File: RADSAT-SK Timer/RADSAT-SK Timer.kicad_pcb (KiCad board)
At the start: 2 copper layers, 90.2 x 95.9 mm, 116 parts, among them J101 Conn_02x26_Odd_Even, J103 Conn_02x26_Odd_Even, J201 Conn_01x07, J202 Conn_01x05, J203 Conn_01x03, J204 Conn_01x02, J205 Conn_01x02, J206 Conn_01x02, J210 ZX62WRD-B-5PC, Q101 IRLML2060, Q102 IRLML2060, Q103 IRLML2060, Q104 IRLML2060, Q105 IRLML2060, Q106 IRLML2060, Q107 IRLML2060, Q108 IRLML2060, Q109 IRLML2060, Q201 IRLML2060, Q202 IRLML2060, Q203 IRLML2060, Q204 PJFET, Q205 PJFET, Q206 PJFET, SW201 SW_Push, SW202 SW_Push, SW203 SW_Push, SW204 SW_Push, SW205 SW_Push, SW206 SW_Push, U101 LM397MF, U102 LM397MF, U103 LM397MF, U104 CD4052B, U202 LTC3440EMSPBF, U210 CPC1117N

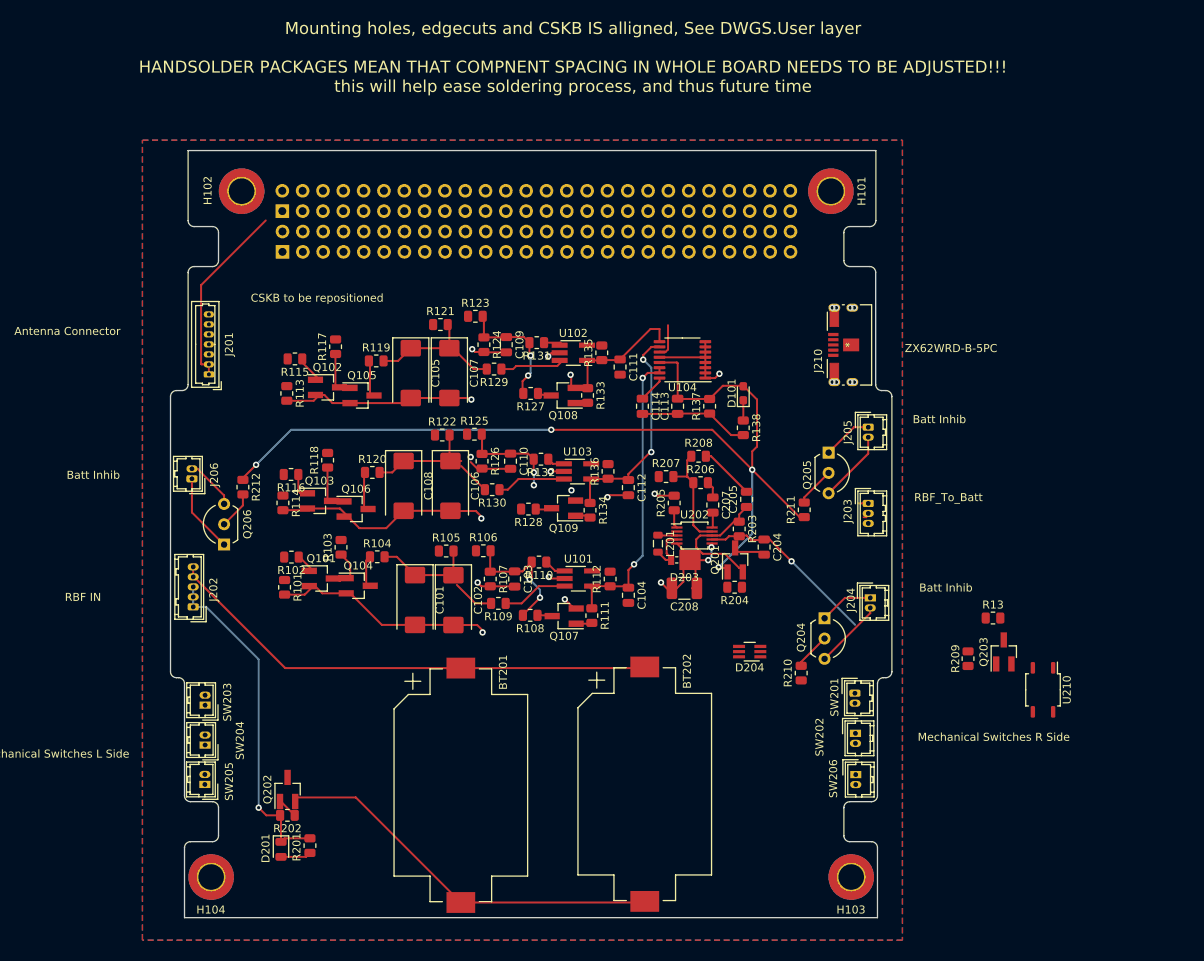
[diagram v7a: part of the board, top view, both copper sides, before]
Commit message: actually did the other relays for the inhibits, played around with layout stuff
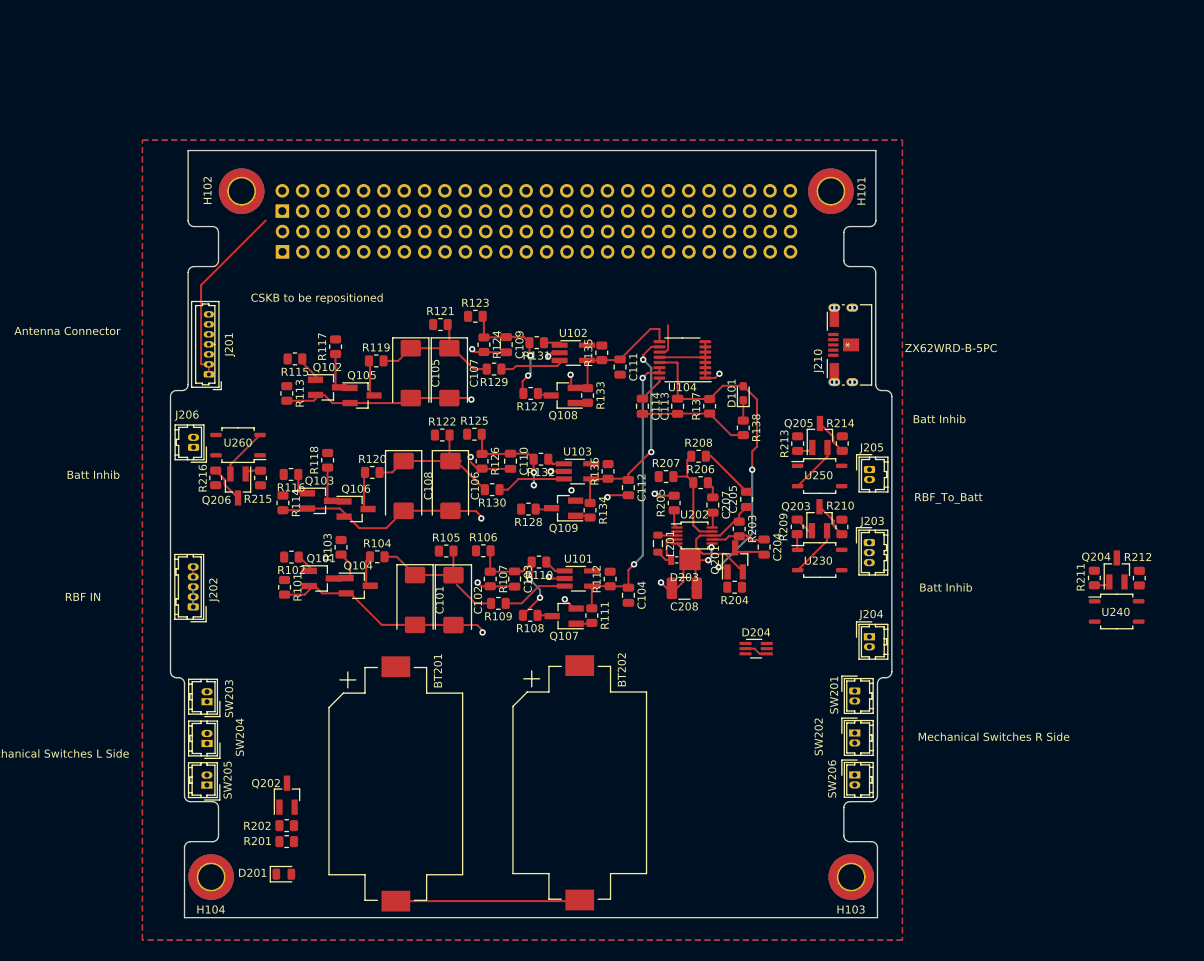
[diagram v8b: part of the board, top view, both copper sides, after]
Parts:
- removed the R210 at (113.7, 115.3)
- added R213: 100, Resistor_SMD:R_0805_2012Metric, F.Cu at (113.2, 86.6)
- added R214: 1k, Resistor_SMD:R_0805_2012Metric, F.Cu at (118.8, 86.6)
- added R215: 100, Resistor_SMD:R_0805_2012Metric, F.Cu at (46.1, 90.9)
- added R216: 1k, Resistor_SMD:R_0805_2012Metric, F.Cu at (40.5, 90.9)
- added U240: CPC1117N, Package_SO:SOP-4_3.8x4.1mm_P2.54mm, F.Cu at (153.1, 107.6)
- added U250: CPC1117N, Package_SO:SOP-4_3.8x4.1mm_P2.54mm, F.Cu at (116.0, 90.7)
- added U260: CPC1117N, Package_SO:SOP-4_3.8x4.1mm_P2.54mm, F.Cu at (43.3, 86.8)
- Q204, Q205, Q206: value PJFET -> IRLML2060; footprint Package_TO_SOT_THT:TO-92L_Inline_Wide -> Package_TO_SOT_SMD:SOT-23_Handsoldering
- R212: value 100 -> 1k
- moved R212 112.6 mm to (155.9, 103.4), turned to 90 degrees
- moved R211 37.3 mm to (150.3, 103.4), turned to 270 degrees
- moved Q204 37.0 mm to (153.1, 102.4), turned to 90 degrees
- moved U230 32.3 mm to (116.0, 101.2), turned to 0 degrees
- moved Q203 28.4 mm to (116.0, 96.0)
- moved R209 27.0 mm to (113.2, 97.0), turned to 90 degrees
- moved R210 22.1 mm to (118.8, 97.1), turned to 90 degrees
- moved BT201 8.13 mm to (63.0, 129.2)
- moved BT202 8.13 mm to (86.0, 129.0)
- moved Q206 7.53 mm to (43.3, 91.9), turned to 270 degrees
- moved J205 5.29 mm to (122.2, 89.9)
- moved J203 4.90 mm to (122.2, 99.0)
- moved J204 4.86 mm to (122.2, 110.8)
- moved J206 3.93 mm to (37.7, 87.1)
- moved D201 3.12 mm to (49.0, 140.5), turned to 0 degrees
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- renumbered R13 to R210, U210 to U230
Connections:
- Q204 pad 1: Net-(J204-Pad1) -> Net-(Q204-Pad1)
- Q204 pad 3: Net-(J204-Pad2) -> Net-(Q204-Pad3)
- Q205 pad 1: Net-(J205-Pad1) -> Net-(Q205-Pad1)
- Q205 pad 3: Net-(J205-Pad2) -> Net-(Q205-Pad3)
- Q206 pad 1: Net-(J206-Pad1) -> Net-(Q206-Pad1)
- Q206 pad 3: Net-(J206-Pad2) -> Net-(Q206-Pad3)
- R210 pad 1: GND -> Net-(Q203-Pad3)
- R210 pad 2: Net-(Q203-Pad3) -> GND
- R211 pad 2: Net-(Q205-Pad2) -> Net-(Q204-Pad1)
- R212 pad 1: BUS_EN -> Net-(Q204-Pad3)
- R212 pad 2: Net-(Q206-Pad2) -> GND
- SW201 pad 1: Net-(C204-Pad1) -> Net-(SW201-Pad1)
- SW201 pad 2: Net-(SW201-Pad2) -> Net-(C204-Pad1)
- SW202 pad 1: Net-(C204-Pad1) -> Net-(SW201-Pad1)
- SW202 pad 2: Net-(SW201-Pad2) -> Net-(C204-Pad1)
- SW203 pad 1: Net-(SW201-Pad2) -> Net-(BT201-Pad1)
- SW203 pad 2: Net-(BT201-Pad1) -> Net-(SW201-Pad1)
- SW204 pad 1: Net-(SW201-Pad2) -> Net-(BT201-Pad1)
- SW204 pad 2: Net-(BT201-Pad1) -> Net-(SW201-Pad1)
- SW205 pad 1: Net-(Q202-Pad3) -> GND
- SW205 pad 2: GND -> Net-(Q202-Pad3)
- SW206 pad 1: Net-(Q202-Pad3) -> GND
- SW206 pad 2: GND -> Net-(Q202-Pad3)
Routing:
- net BUS_EN: track 119.6 -> 42.2 mm, vias 4 -> 2
- net Net-(BT201-Pad1): track 62.5 -> 1.25 mm
- net Net-(D201-Pad1): track 42.2 -> 2.50 mm, vias 1 -> 0
- net Net-(BT201-Pad2): track 49.2 -> 23.0 mm
- net Net-(C204-Pad1): track 22.7 -> 6.88 mm, vias 1 -> 0
- net Net-(J206-Pad1): track 9.89 -> 0.00 mm
- net Net-(J205-Pad2): track 9.06 -> 0.00 mm
- net Net-(J204-Pad2): track 8.74 -> 0.00 mm
- net Net-(J204-Pad1): track 6.77 -> 0.00 mm
- net Net-(J206-Pad2): track 6.46 -> 0.00 mm
- net Net-(Q203-Pad2): track 0.00 -> 6.45 mm
- net Net-(J205-Pad1): track 6.27 -> 0.00 mm
- net Net-(Q204-Pad2): track 4.62 -> 0.00 mm
- net Net-(Q203-Pad3): track 0.00 -> 4.60 mm
- net Net-(Q205-Pad3): track 0.00 -> 4.58 mm
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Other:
- board text removed: "Mounting holes, edgecuts and CSKB IS alligned, See DWGS.User layer HANDSOLDER PACKAGES MEAN THAT COMPNENT SPACING IN WHOLE BOARD NEEDS TO BE ADJUSTED!!! this will help ease soldering process, and thus future time"
